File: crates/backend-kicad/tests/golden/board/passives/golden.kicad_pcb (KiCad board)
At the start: 2 copper layers, 100 x 80 mm, 5 parts, among them Y1 Y

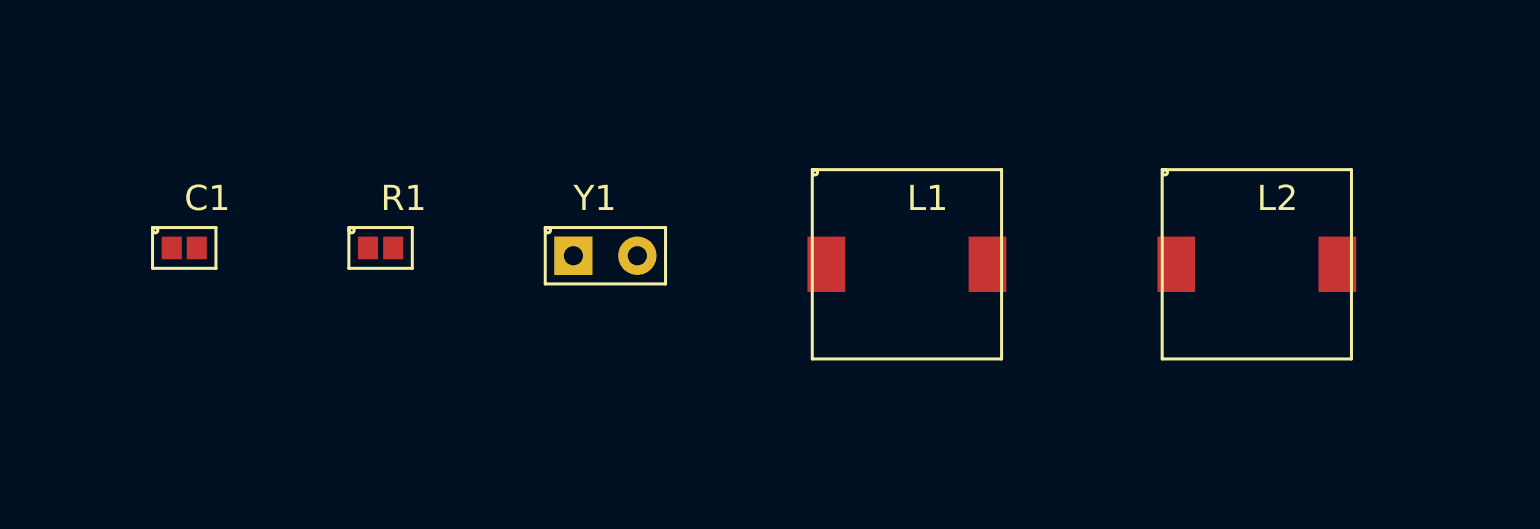
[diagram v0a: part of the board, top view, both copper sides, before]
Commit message: Fix bugs with footprints and DRC rules
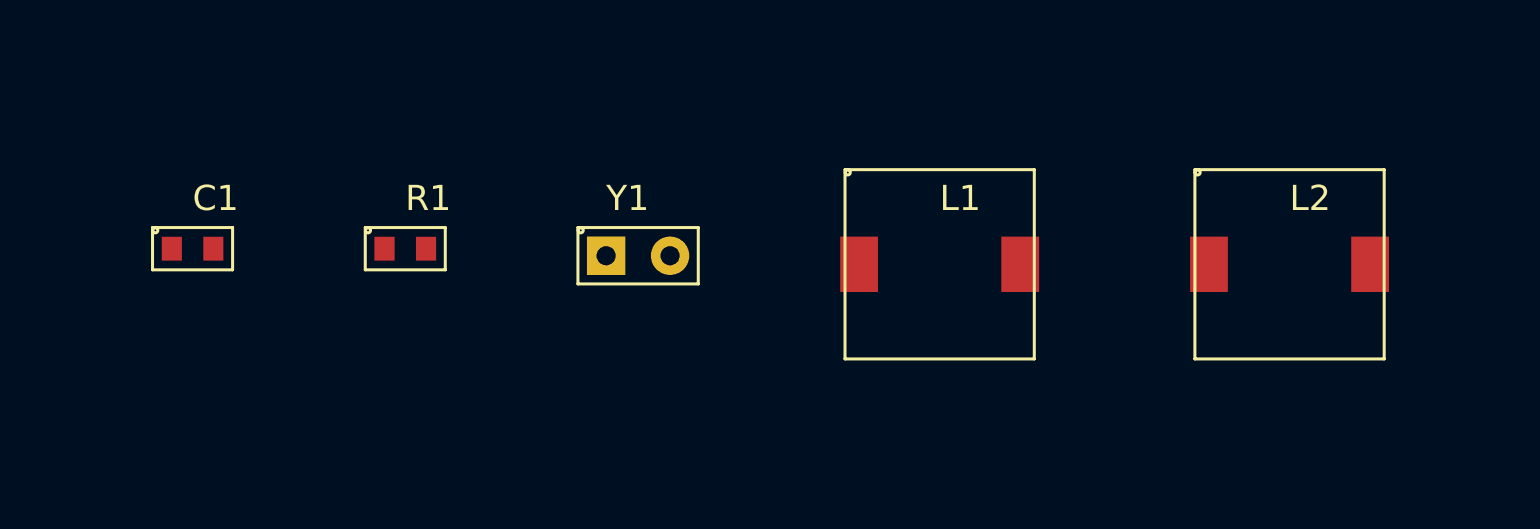
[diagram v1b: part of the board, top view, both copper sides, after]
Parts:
- moved L2 1.30 mm to (55.3, 11.6)
- moved Y1 1.30 mm to (28.2, 11.3)
- moved L1 1.30 mm to (41.4, 11.6)
- moved R1 0.98 mm to (20.2, 11.0)
- moved C1 0.33 mm to (11.7, 11.0)
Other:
- net class Default: trace_width 0.25 -> 0.2
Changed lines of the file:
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@@
   (net_class "Default" ""
     (clearance 0.2)
-    (trace_width 0.25)
+    (trace_width 0.2)
     (via_dia 0.8)
     (via_drill 0.4)
@@
     (layer "F.Cu")
     (locked no)
-    (at 11.4 10.95 0)
+    (at 11.73 10.98 0)
     (property "Reference" "C1"
-      (at 0 -1.97 0)
+      (at 0 -2 0)
       (layer "F.SilkS")
       (effects
@@
         (justify left)))
     (property "Value" "C"
-      (at 0 1.97 0)
+      (at 0 2 0)
       (layer "F.SilkS")
       (hide yes)
@@
         (justify left)))
     (fp_text user "${VALUE}"
-      (at 0 1.97)
+      (at 0 2)
       (layer F.Fab)
       (effects
@@
     (attr smd)
     (fp_line
-      (start -1.15 -0.7)
-      (end 1.15 -0.7)
-      (layer F.Fab)
-      (width 0.1)
-)
-    (fp_line
-      (start 1.15 -0.7)
-      (end 1.15 0.7)
-      (layer F.Fab)
-      (width 0.1)
-)
-    (fp_line
-      (start 1.15 0.7)
-      (end -1.15 0.7)
-      (layer F.Fab)
-      (width 0.1)
-)
-    (fp_line
-      (start -1.15 0.7)
-      (end -1.15 -0.7)
-      (layer F.Fab)
-      (width 0.1)
-)
-    (fp_line
-      (start -1.26 -0.81)
-      (end 1.26 -0.81)
-      (layer F.SilkS)
-      (width 0.12)
-)
-    (fp_line
-      (start 1.26 -0.81)
-      (end 1.26 0.81)
-      (layer F.SilkS)
-      (width 0.12)
-)
-    (fp_line
-      (start 1.26 0.81)
-      (end -1.26 0.81)
-      (layer F.SilkS)
-      (width 0.12)
-)
-    (fp_line
-      (start -1.26 0.81)
-      (end -1.26 -0.81)
-      (layer F.SilkS)
-      (width 0.12)
-)
-    (fp_line
-      (start -1.4 -0.95)
-      (end 1.4 -0.95)
-      (layer F.CrtYd)
-      (width 0.05)
-)
-    (fp_line
-      (start 1.4 -0.95)
-      (end 1.4 0.95)
-      (layer F.CrtYd)
-      (width 0.05)
-)
-    (fp_line
-      (start 1.4 0.95)
-      (end -1.4 0.95)
-      (layer F.CrtYd)
-      (width 0.05)
-)
-    (fp_line
-      (start -1.4 0.95)
-      (end -1.4 -0.95)
+      (start -1.48 -0.73)
+      (end 1.48 -0.73)
+      (layer F.Fab)
+      (width 0.1)
+)
+    (fp_line
+      (start 1.48 -0.73)
+      (end 1.48 0.73)
+      (layer F.Fab)
+      (width 0.1)
+)
+    (fp_line
+      (start 1.48 0.73)
+      (end -1.48 0.73)
+      (layer F.Fab)
+      (width 0.1)
+)
+    (fp_line
+      (start -1.48 0.73)
+      (end -1.48 -0.73)
+      (layer F.Fab)
+      (width 0.1)
+)
+    (fp_line
+      (start -1.59 -0.84)
+      (end 1.59 -0.84)
+      (layer F.SilkS)
+      (width 0.12)
+)
+    (fp_line
+      (start 1.59 -0.84)
+      (end 1.59 0.84)
+      (layer F.SilkS)
+      (width 0.12)
+)
+    (fp_line
+      (start 1.59 0.84)
+      (end -1.59 0.84)
+      (layer F.SilkS)
+      (width 0.12)
+)
+    (fp_line
+      (start -1.59 0.84)
+      (end -1.59 -0.84)
+      (layer F.SilkS)
+      (width 0.12)
+)
+    (fp_line
+      (start -1.73 -0.98)
+      (end 1.73 -0.98)
+      (layer F.CrtYd)
+      (width 0.05)
+)
+    (fp_line
+      (start 1.73 -0.98)
+      (end 1.73 0.98)
+      (layer F.CrtYd)
+      (width 0.05)
+)
+    (fp_line
+      (start 1.73 0.98)
+      (end -1.73 0.98)
+      (layer F.CrtYd)
+      (width 0.05)
+)
+    (fp_line
+      (start -1.73 0.98)
+      (end -1.73 -0.98)
       (layer F.CrtYd)
       (width 0.05)
 )
     (fp_circle
-      (center -1.15 -0.7)
-      (end -1.05 -0.7)
+      (center -1.48 -0.73)
+      (end -1.38 -0.73)
       (layer F.SilkS)
       (width 0.12)
 )
     (pad "1" smd rect
-      (at -0.5 0)
-      (size 0.8 0.9)
+      (at -0.825 0)
+      (size 0.8 0.95)
       (layers F.Cu F.Mask F.Paste)
 )
     (pad "2" smd rect
-      (at 0.5 0)
-      (size 0.8 0.9)
+      (at 0.825 0)
+      (size 0.8 0.95)
       (layers F.Cu F.Mask F.Paste)
 )
@@
     (layer "F.Cu")
     (locked no)
-    (at 19.2 10.95 0)
+    (at 20.18 10.98 0)
     (property "Reference" "R1"
-      (at 0 -1.97 0)
+      (at 0 -2 0)
       (layer "F.SilkS")
       (effects
@@
         (justify left)))
     (property "Value" "R"
-      (at 0 1.97 0)
+      (at 0 2 0)
       (layer "F.SilkS")
       (hide yes)
@@
         (justify left)))
     (fp_text user "${VALUE}"
-      (at 0 1.97)
+      (at 0 2)
       (layer F.Fab)
       (effects
@@
     (attr smd)
     (fp_line
-      (start -1.15 -0.7)
-      (end 1.15 -0.7)
-      (layer F.Fab)
-      (width 0.1)
-)
-    (fp_line
-      (start 1.15 -0.7)
-      (end 1.15 0.7)
-      (layer F.Fab)
-      (width 0.1)
-)
-    (fp_line
-      (start 1.15 0.7)
-      (end -1.15 0.7)
-      (layer F.Fab)
-      (width 0.1)
-)
-    (fp_line
-      (start -1.15 0.7)
-      (end -1.15 -0.7)
-      (layer F.Fab)
-      (width 0.1)
-)
-    (fp_line
-      (start -1.26 -0.81)
-      (end 1.26 -0.81)
-      (layer F.SilkS)
-      (width 0.12)
-)
-    (fp_line
-      (start 1.26 -0.81)
-      (end 1.26 0.81)
-      (layer F.SilkS)
-      (width 0.12)
-)
-    (fp_line
-      (start 1.26 0.81)
-      (end -1.26 0.81)
-      (layer F.SilkS)
-      (width 0.12)
-)
-    (fp_line
-      (start -1.26 0.81)
-      (end -1.26 -0.81)
-      (layer F.SilkS)
-      (width 0.12)
-)
-    (fp_line
-      (start -1.4 -0.95)
-      (end 1.4 -0.95)
-      (layer F.CrtYd)
-      (width 0.05)
-)
-    (fp_line
-      (start 1.4 -0.95)
-      (end 1.4 0.95)
-      (layer F.CrtYd)
-      (width 0.05)
-)
-    (fp_line
-      (start 1.4 0.95)
-      (end -1.4 0.95)
-      (layer F.CrtYd)
-      (width 0.05)
-)
-    (fp_line
-      (start -1.4 0.95)
-      (end -1.4 -0.95)
+      (start -1.48 -0.73)
+      (end 1.48 -0.73)
+      (layer F.Fab)
+      (width 0.1)
+)
+    (fp_line
+      (start 1.48 -0.73)
+      (end 1.48 0.73)
+      (layer F.Fab)
+      (width 0.1)
+)
+    (fp_line
+      (start 1.48 0.73)
+      (end -1.48 0.73)
+      (layer F.Fab)
+      (width 0.1)
+)
+    (fp_line
+      (start -1.48 0.73)
+      (end -1.48 -0.73)
+      (layer F.Fab)
+      (width 0.1)
+)
+    (fp_line
+      (start -1.59 -0.84)
+      (end 1.59 -0.84)
+      (layer F.SilkS)
+      (width 0.12)
+)
+    (fp_line
+      (start 1.59 -0.84)
+      (end 1.59 0.84)
+      (layer F.SilkS)
+      (width 0.12)
+)
+    (fp_line
+      (start 1.59 0.84)
+      (end -1.59 0.84)
+      (layer F.SilkS)
+      (width 0.12)
+)
+    (fp_line
+      (start -1.59 0.84)
+      (end -1.59 -0.84)
+      (layer F.SilkS)
+      (width 0.12)
+)
+    (fp_line
+      (start -1.73 -0.98)
+      (end 1.73 -0.98)
+      (layer F.CrtYd)
+      (width 0.05)
+)
+    (fp_line
+      (start 1.73 -0.98)
+      (end 1.73 0.98)
+      (layer F.CrtYd)
+      (width 0.05)
+)
+    (fp_line
+      (start 1.73 0.98)
+      (end -1.73 0.98)
+      (layer F.CrtYd)
+      (width 0.05)
+)
+    (fp_line
+      (start -1.73 0.98)
+      (end -1.73 -0.98)
       (layer F.CrtYd)
       (width 0.05)
 )
     (fp_circle
-      (center -1.15 -0.7)
-      (end -1.05 -0.7)
+      (center -1.48 -0.73)
+      (end -1.38 -0.73)
       (layer F.SilkS)
       (width 0.12)
 )
     (pad "1" smd rect
-      (at -0.5 0)
-      (size 0.8 0.9)
+      (at -0.825 0)
+      (size 0.8 0.95)
       (layers F.Cu F.Mask F.Paste)
 )
     (pad "2" smd rect
-      (at 0.5 0)
-      (size 0.8 0.9)
+      (at 0.825 0)
+      (size 0.8 0.95)
       (layers F.Cu F.Mask F.Paste)
 )
@@
     (layer "F.Cu")
     (locked no)
-    (at 26.86 11.26 0)
+    (at 28.16 11.26 0)
     (property "Reference" "Y1"
       (at 0 -2.28 0)
@@
     (layer "F.Cu")
     (locked no)
-    (at 40.11 11.6 0)
+    (at 41.41 11.6 0)
     (property "Reference" "L1"
       (at 0 -2.62 0)
@@
     (layer "F.Cu")
     (locked no)
-    (at 54.01 11.6 0)
+    (at 55.31 11.6 0)
     (property "Reference" "L2"
       (at 0 -2.62 0)
